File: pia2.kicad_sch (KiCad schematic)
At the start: 41 parts, among them IC25 LM393, IC31 74LS02, IC34 MC14050BCP, IC35 MC6821

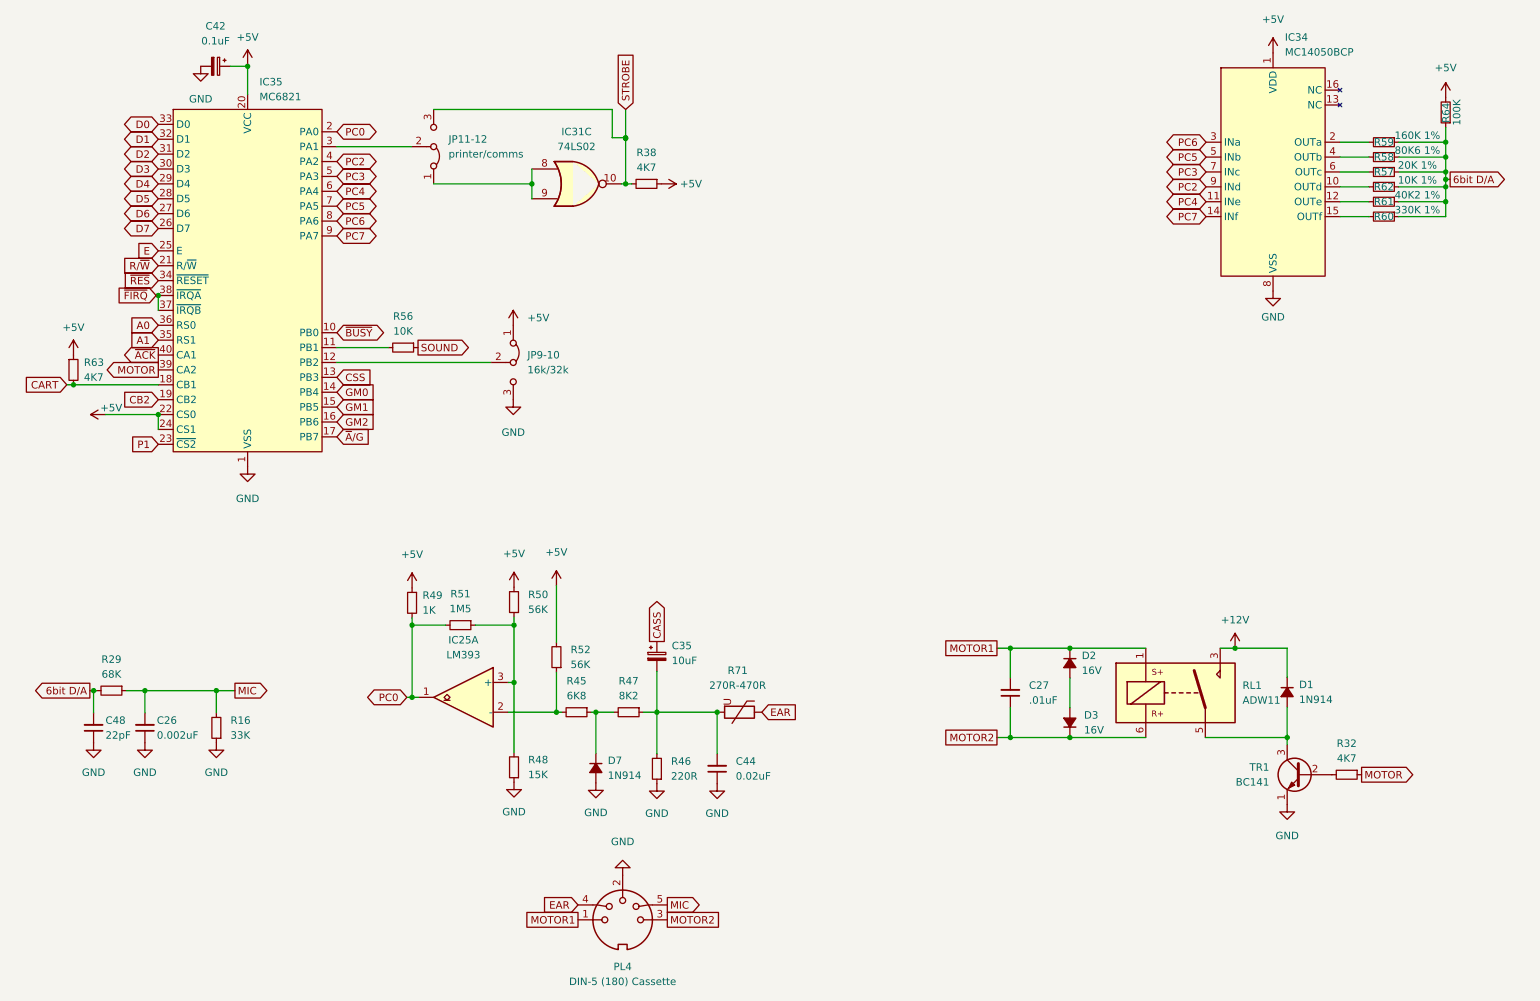
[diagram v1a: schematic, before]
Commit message: validate component values
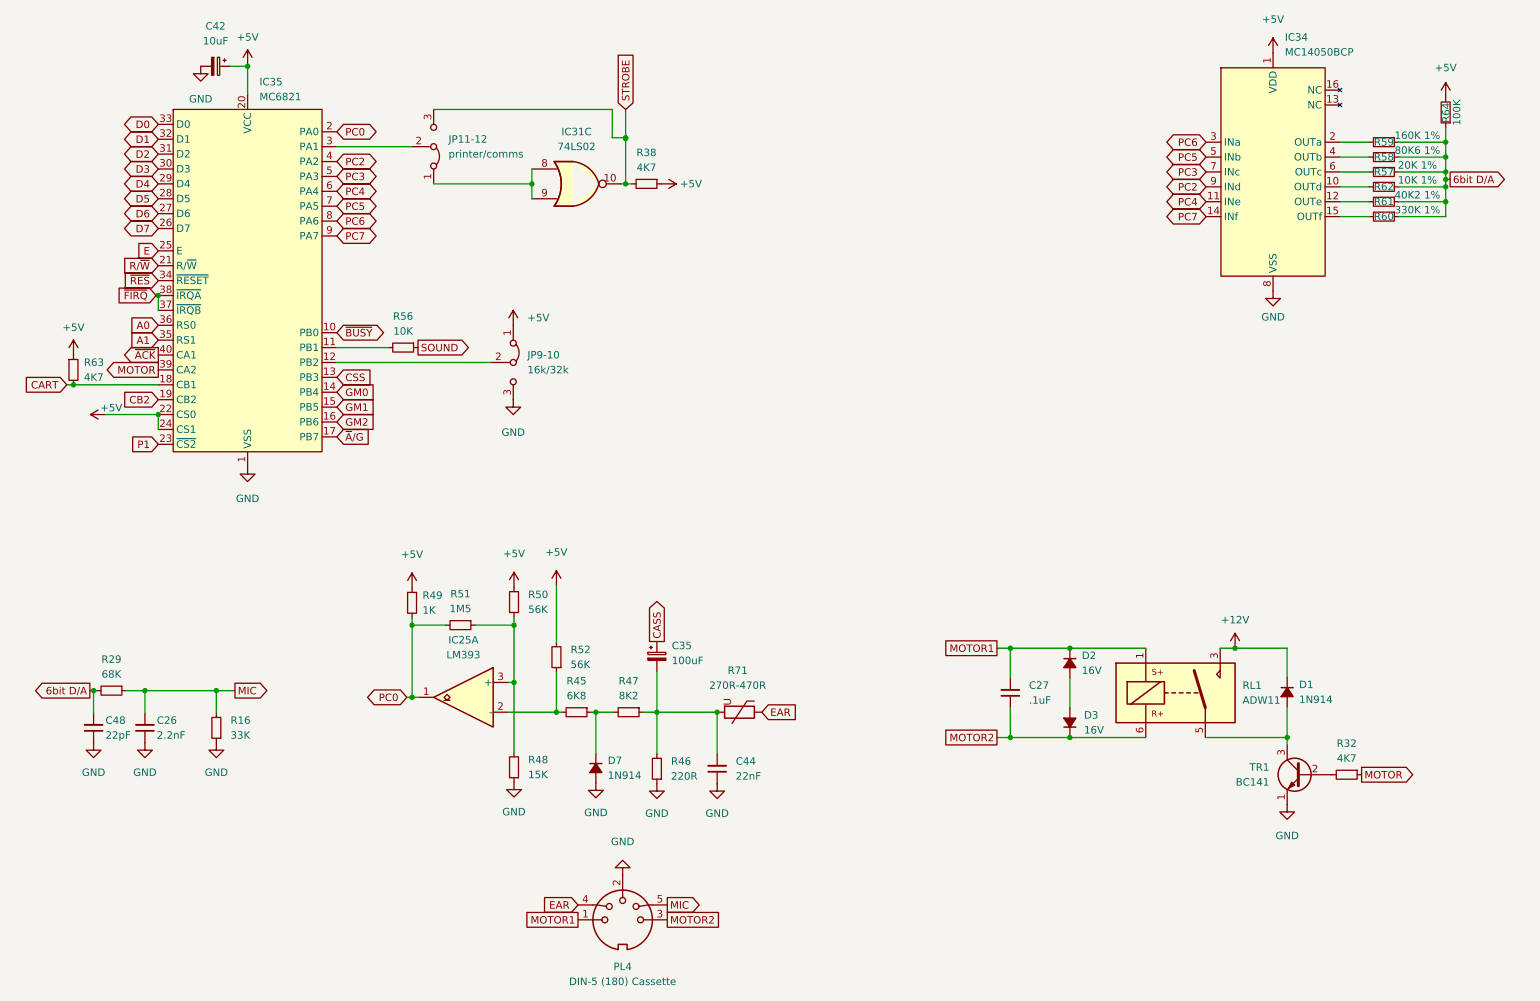
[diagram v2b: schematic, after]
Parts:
- C26: value 0.002uF -> 2.2nF; DigiKey (none) -> BC1074CT-ND
- C27: value .01uF -> .1uF; footprint Capacitor_THT:C_Disc_D3.0mm_W2.0mm_P2.50mm -> Capacitor_THT:C_Disc_D4.3mm_W1.9mm_P5.00mm
- C35: value 10uF -> 100uF; DigiKey (none) -> 732-8598-1-ND
- C42: value 0.1uF -> 10uF; DigiKey (none) -> 732-8593-1-ND
- C44: value 0.02uF -> 22nF; footprint Capacitor_THT:C_Disc_D3.0mm_W2.0mm_P2.50mm -> Capacitor_THT:C_Disc_D5.0mm_W2.5mm_P5.00mm; DigiKey (none) -> BC2677CT-ND
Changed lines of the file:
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@@
       (effects (font (size 1.27 1.27)) (justify right))
     )
-    (property "Value" ".01uF" (id 1) (at 193.04 134.6135 0)
-      (effects (font (size 1.27 1.27)) (justify right))
-    )
-    (property "Footprint" "Capacitor_THT:C_Disc_D3.0mm_W2.0mm_P2.50mm" (id 2) (at 189.865 133.35 0)
+    (property "Value" ".1uF" (id 1) (at 193.04 134.6135 0)
+      (effects (font (size 1.27 1.27)) (justify right))
+    )
+    (property "Footprint" "Capacitor_THT:C_Disc_D4.3mm_W1.9mm_P5.00mm" (id 2) (at 189.865 133.35 0)
       (effects (font (size 1.27 1.27)) hide)
     )
@@
       (effects (font (size 1.27 1.27)) (justify right))
     )
-    (property "Value" "0.002uF" (id 1) (at 44.196 140.589 0)
+    (property "Value" "2.2nF" (id 1) (at 44.196 140.589 0)
       (effects (font (size 1.27 1.27)) (justify right))
     )
@@
       (effects (font (size 1.27 1.27)) hide)
     )
-    (property "Datasheet" "~" (id 3) (at 42.164 139.319 0)
+    (property "Datasheet" "https://www.vishay.com/docs/45171/kseries.pdf" (id 3) (at 42.164 139.319 0)
+      (effects (font (size 1.27 1.27)) hide)
+    )
+    (property "DigiKey" "BC1074CT-ND" (id 4) (at 42.164 139.319 0)
       (effects (font (size 1.27 1.27)) hide)
     )
@@
     (in_bom yes) (on_board yes) (fields_autoplaced)
     (property "Reference" "C42" (id 0) (at 54.2226 19.558 90))
-    (property "Value" "0.1uF" (id 1) (at 54.2226 22.098 90))
+    (property "Value" "10uF" (id 1) (at 54.2226 22.098 90))
     (property "Footprint" "Capacitor_THT:CP_Radial_D5.0mm_P2.50mm" (id 2) (at 54.229 26.416 0)
       (effects (font (size 1.27 1.27)) hide)
     )
-    (property "Datasheet" "~" (id 3) (at 54.229 26.416 0)
+    (property "Datasheet" "https://www.we-online.com/katalog/datasheet/860010372001.pdf" (id 3) (at 54.229 26.416 0)
+      (effects (font (size 1.27 1.27)) hide)
+    )
+    (property "DigiKey" "732-8593-1-ND" (id 4) (at 54.229 26.416 90)
       (effects (font (size 1.27 1.27)) hide)
     )
@@
       (effects (font (size 1.27 1.27)) (justify right))
     )
-    (property "Value" "0.02uF" (id 1) (at 143.002 147.5675 0)
-      (effects (font (size 1.27 1.27)) (justify right))
-    )
-    (property "Footprint" "Capacitor_THT:C_Disc_D3.0mm_W2.0mm_P2.50mm" (id 2) (at 139.827 146.304 0)
-      (effects (font (size 1.27 1.27)) hide)
-    )
-    (property "Datasheet" "~" (id 3) (at 139.827 146.304 0)
+    (property "Value" "22nF" (id 1) (at 143.002 147.5675 0)
+      (effects (font (size 1.27 1.27)) (justify right))
+    )
+    (property "Footprint" "Capacitor_THT:C_Disc_D5.0mm_W2.5mm_P5.00mm" (id 2) (at 139.827 146.304 0)
+      (effects (font (size 1.27 1.27)) hide)
+    )
+    (property "Datasheet" "https://www.vishay.com/docs/45171/kseries.pdf" (id 3) (at 139.827 146.304 0)
+      (effects (font (size 1.27 1.27)) hide)
+    )
+    (property "DigiKey" "BC2677CT-ND" (id 4) (at 139.827 146.304 0)
       (effects (font (size 1.27 1.27)) hide)
     )
@@
       (effects (font (size 1.27 1.27)) hide)
     )
-    (pin "1")
-    (pin "2")
-    (pin "3")
-    (pin "4")
-    (pin "5")
-    (pin "6")
     (pin "10")
     (pin "8")
     (pin "9")
-    (pin "11")
-    (pin "12")
-    (pin "13")
-    (pin "14")
-    (pin "7")
   )
   (symbol (lib_id "Jumper:Jumper_3_Bridged12") (at 91.44 40.132 270) (mirror x) (unit 1)
@@
     (pin "2")
     (pin "3")
-    (pin "5")
-    (pin "6")
-    (pin "7")
-    (pin "4")
-    (pin "8")
   )
   (symbol (lib_id "Device:R_Small") (at 36.449 132.969 270) (unit 1)
@@
       (effects (font (size 1.27 1.27)) (justify left))
     )
-    (property "Value" "10uF" (id 1) (at 132.08 127.8508 0)
+    (property "Value" "100uF" (id 1) (at 132.08 127.8508 0)
       (effects (font (size 1.27 1.27)) (justify left))
     )
@@
       (effects (font (size 1.27 1.27)) hide)
     )
-    (property "Datasheet" "~" (id 3) (at 129.54 127.127 0)
-      (effects (font (size 1.27 1.27)) hide)
-    )
+    (property "Datasheet" "https://www.we-online.com/katalog/datasheet/860010372006.pdf" (id 3) (at 129.54 127.127 0)
+      (effects (font (size 1.27 1.27)) hide)
+    )
+    (property "DigiKey" "732-8598-1-ND" (id 4) (at 129.54 127.127 0)
+      (effects (font (size 1.27 1.27)) hide)
+    )

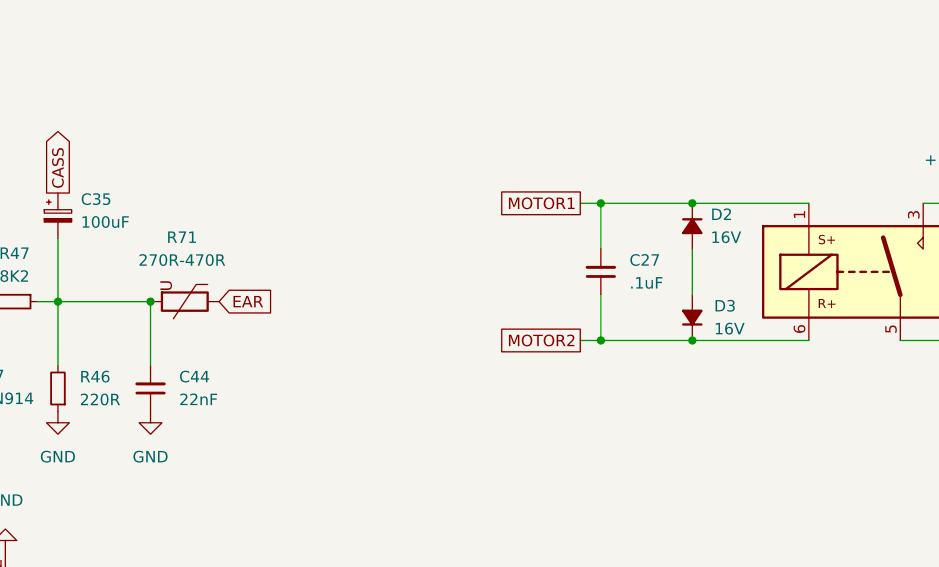
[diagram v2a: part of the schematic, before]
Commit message: complete component revision
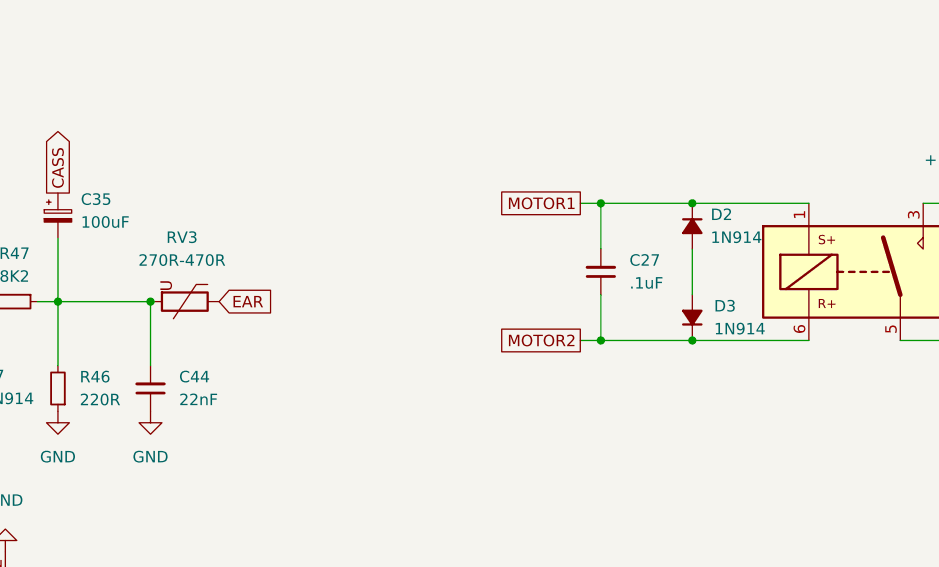
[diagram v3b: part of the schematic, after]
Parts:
- D2, D3: value 16V -> 1N914
- renumbered R71 to RV3
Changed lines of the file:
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@@
       (effects (font (size 1.27 1.27)) (justify left))
     )
-    (property "Value" "16V" (id 1) (at 202.057 129.5399 90)
+    (property "Value" "1N914" (id 1) (at 202.057 129.5399 90)
       (effects (font (size 1.27 1.27)) (justify left))
     )
@@
       (effects (font (size 1.27 1.27)) (justify left))
     )
-    (property "Value" "16V" (id 1) (at 202.438 139.6999 90)
+    (property "Value" "1N914" (id 1) (at 202.438 139.6999 90)
       (effects (font (size 1.27 1.27)) (justify left))
     )
@@
   (symbol (lib_id "Device:Varistor") (at 143.637 136.652 270) (unit 1)
     (in_bom yes) (on_board yes) (fields_autoplaced)
-    (property "Reference" "R71" (id 0) (at 143.3242 129.54 90))
+    (property "Reference" "RV3" (id 0) (at 143.3242 129.54 90))
     (property "Value" "270R-470R" (id 1) (at 143.3242 132.08 90))
     (property "Footprint" "Varistor:RV_Disc_D7mm_W3.4mm_P5mm" (id 2) (at 143.637 134.874 90)

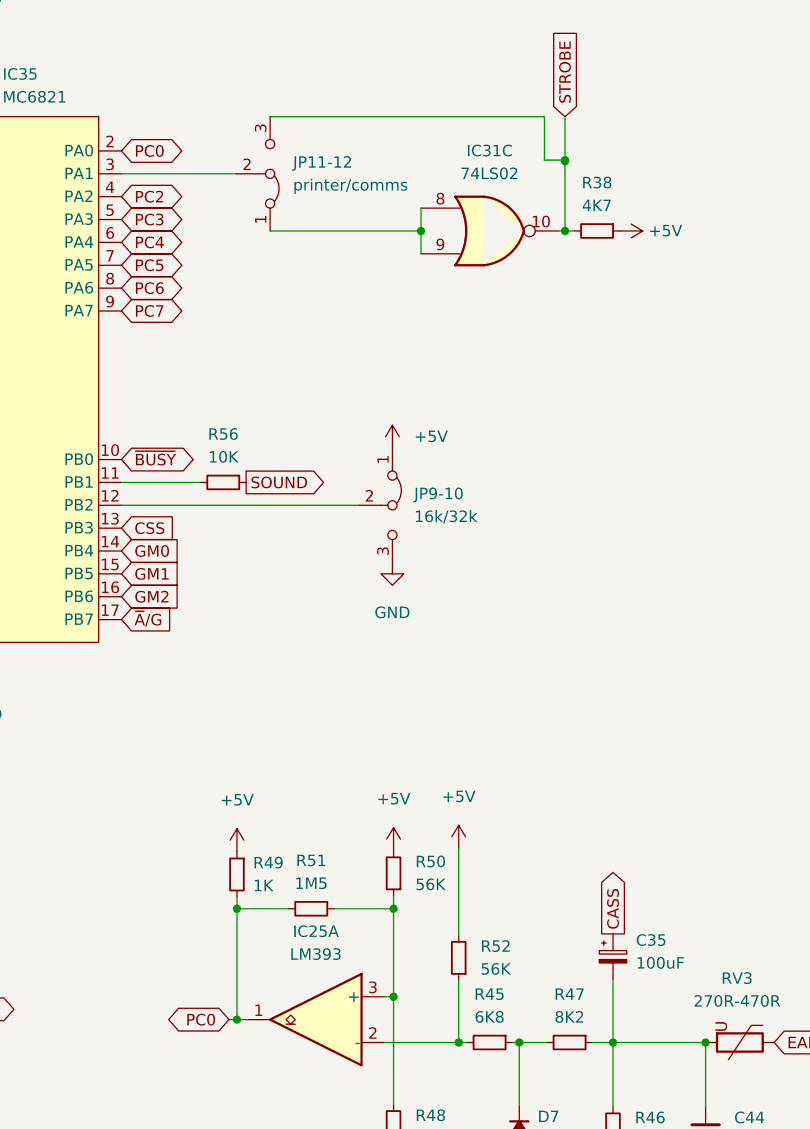
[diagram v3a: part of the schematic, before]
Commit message: cross-reference items to suppliers
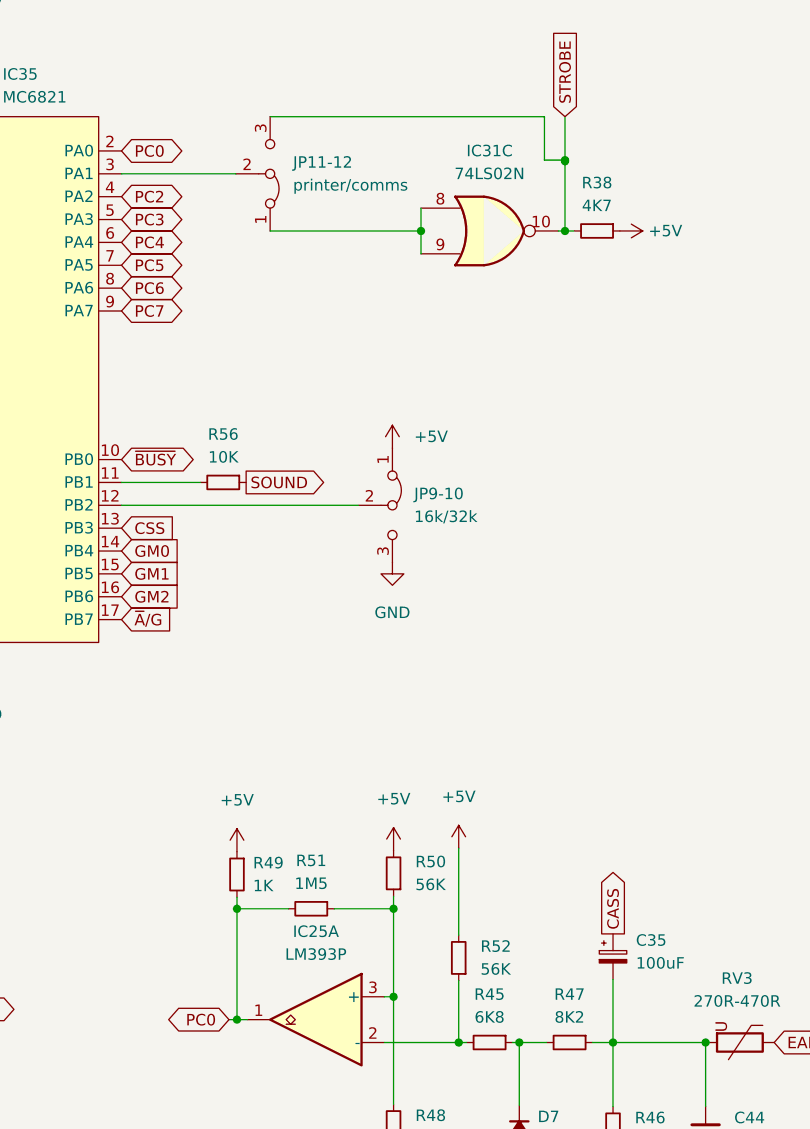
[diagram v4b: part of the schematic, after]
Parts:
- IC25: value LM393 -> LM393P
- IC31: value 74LS02 -> 74LS02N
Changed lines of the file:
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@@
       (effects (font (size 1.27 1.27)) hide)
     )
-    (property "Datasheet" "" (id 3) (at 123.698 172.085 0)
+    (property "Datasheet" "https://www.dem-uk.com/deltron-components/Data/Product_Downloads/deltron-671-0501-5-way-din-socket-data.pdf" (id 3) (at 123.698 172.085 0)
       (effects (font (size 1.27 1.27)) hide)
     )
@@
       (effects (font (size 1.27 1.27)) hide)
     )
-    (property "Datasheet" "" (id 3) (at 234.696 53.34 0)
+    (property "Datasheet" "https://media.digikey.com/pdf/Data%20Sheets/ON%20Semiconductor%20PDFs/MC14049B,50B_Rev7.pdf" (id 3) (at 234.696 53.34 0)
       (effects (font (size 1.27 1.27)) hide)
     )
@@
     (in_bom yes) (on_board yes) (fields_autoplaced)
     (property "Reference" "IC31" (id 0) (at 115.824 37.592 0))
-    (property "Value" "74LS02" (id 1) (at 115.824 40.132 0))
+    (property "Value" "74LS02N" (id 1) (at 115.824 40.132 0))
     (property "Footprint" "Package_DIP:DIP-14_W7.62mm" (id 2) (at 115.824 46.482 0)
       (effects (font (size 1.27 1.27)) hide)
@@
     (in_bom yes) (on_board yes) (fields_autoplaced)
     (property "Reference" "IC25" (id 0) (at 96.52 124.333 0))
-    (property "Value" "LM393" (id 1) (at 96.52 126.873 0))
+    (property "Value" "LM393P" (id 1) (at 96.52 126.873 0))
     (property "Footprint" "Package_DIP:DIP-8_W7.62mm" (id 2) (at 96.52 134.112 0)
       (effects (font (size 1.27 1.27)) hide)
